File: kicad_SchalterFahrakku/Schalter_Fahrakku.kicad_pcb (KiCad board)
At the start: 2 copper layers, 55 x 25 mm, 63 parts, among them P1 V_IN+, P2 V_IN-, P3 uC_IN, P4 V_OUT+, P5 V_OUT-, Q1 IRLML6344, Q2 IPD90P03

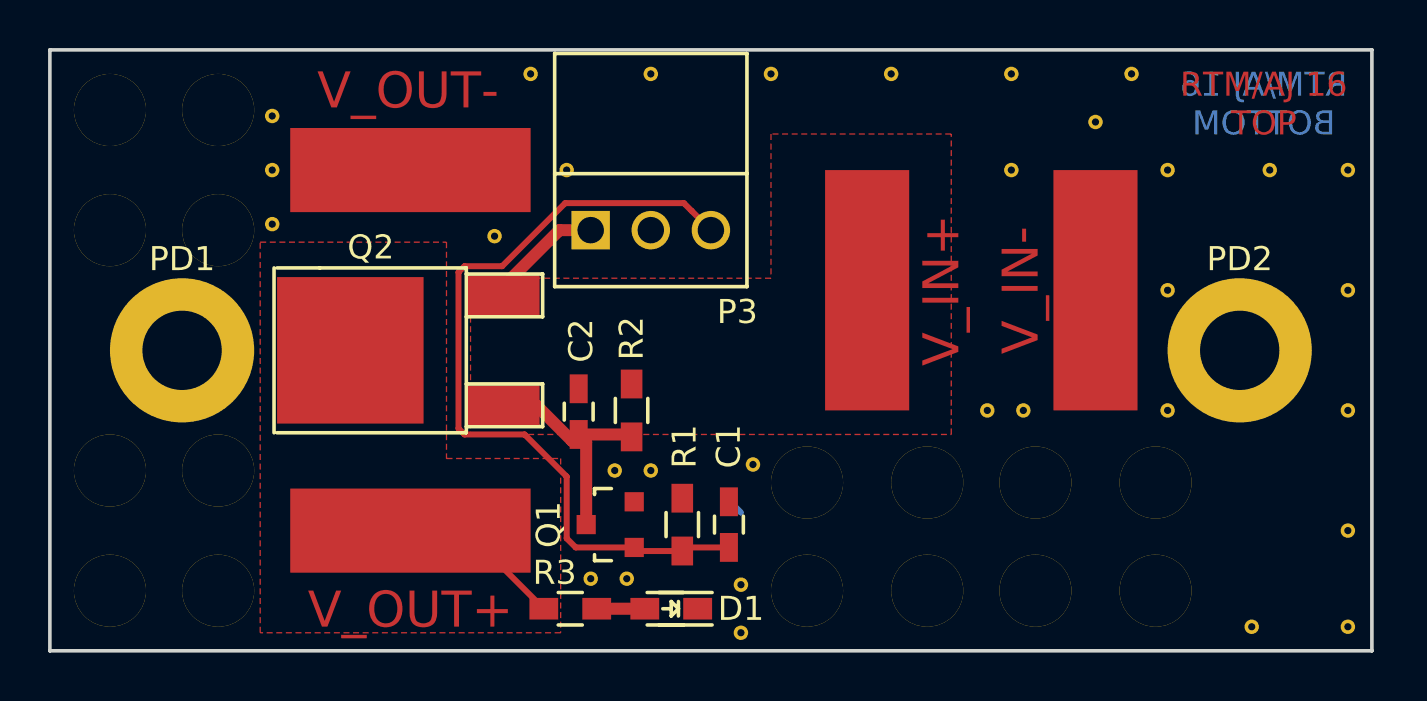
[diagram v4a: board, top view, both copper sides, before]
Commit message: - Pinzuordnung bei Winkelstecker geändert - Platinenbezeichnung in Kupfer eingebettet
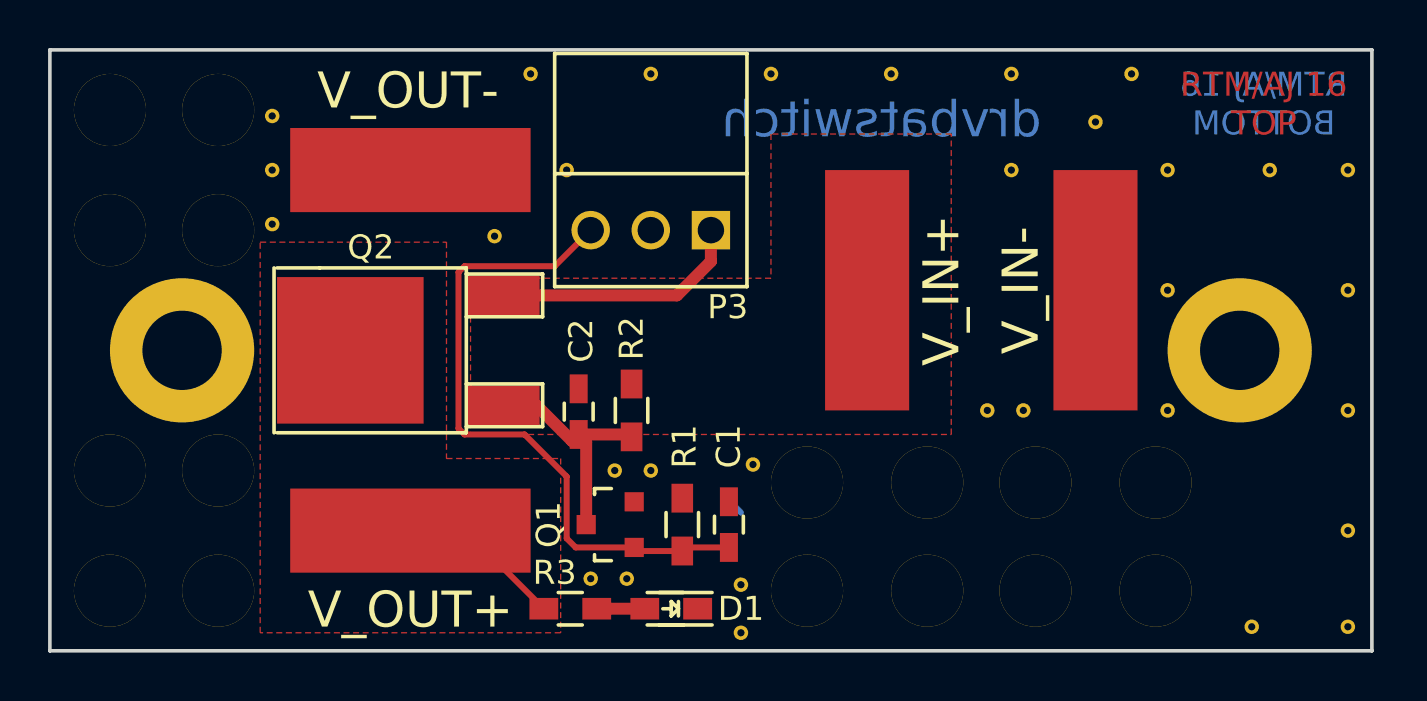
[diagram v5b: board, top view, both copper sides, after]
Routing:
- net Net-(C2-Pad1): track 4.13 -> 10.5 mm
- net /CTL_DRIVE: track 33.6 -> 27.7 mm
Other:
- board text added: "drvbatswitch"

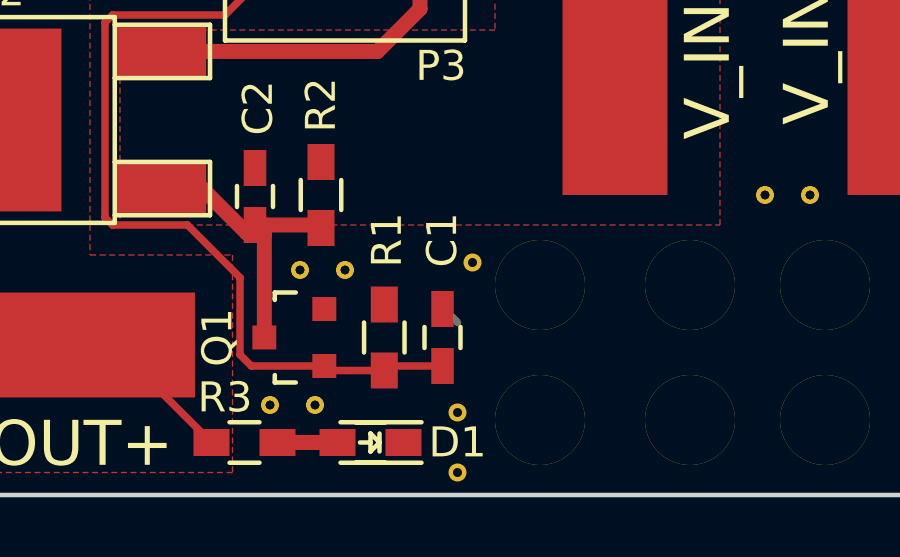
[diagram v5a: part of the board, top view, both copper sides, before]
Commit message: Stub auf Unterseite entfernt
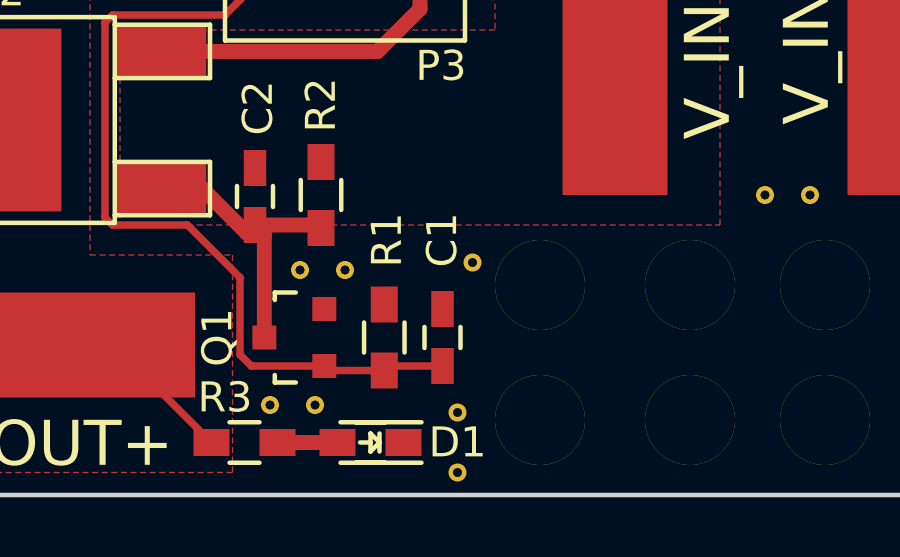
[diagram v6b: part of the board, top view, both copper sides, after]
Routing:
- net (no net): track 0.71 -> 0.00 mm
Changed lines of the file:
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@@
     (links 51)
     (no_connects 0)
-    (area 99.924999 69.924999 155.075001 95.075001)
+    (area 87.150001 69.225 155.075001 115.300001)
     (thickness 1.6)
     (drawings 14)
-    (tracks 28)
+    (tracks 27)
     (zones 0)
     (modules 63)
@@
     (visible_elements 7FFFFFFF)
     (pcbplotparams
-      (layerselection 0x00030_80000001)
+      (layerselection 0x010f0_80000001)
       (usegerberextensions false)
       (excludeedgelayer true)
       (linewidth 0.100000)
       (plotframeref false)
-      (viasonmask false)
+      (viasonmask true)
       (mode 1)
       (useauxorigin false)
@@
       (outputformat 1)
       (mirror false)
-      (drillshape 1)
+      (drillshape 0)
       (scaleselection 1)
-      (outputdirectory ""))
+      (outputdirectory ../mfg/))
   )
   (net 0 "")
@@
   (gr_line (start 100 95) (end 155 95) (layer Edge.Cuts) (width 0.15))
   (gr_line (start 100 70) (end 100 95) (layer Edge.Cuts) (width 0.15))
-  (segment (start 128.75 89.25) (end 128.25 88.75) (width 0.25) (layer B.Cu) (net 0))
   (segment (start 124.31076 90.7) (end 121.876678 90.7) (width 0.25) (layer F.Cu) (net 1))
   (segment (start 117.25 79) (end 121 79) (width 0.25) (layer F.Cu) (net 1))
